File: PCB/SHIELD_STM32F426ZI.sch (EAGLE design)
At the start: 16 parts, among them IC1 AS4C16M16SA-6TCN

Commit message: Namen der DCMI-Pins hinzufügen und Position des Kondensators korrigieren
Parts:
- renumbered IC1 to SDRAM, STM32F4 to STM32

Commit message: new update
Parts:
- CAMERA, JP2, JP3: value (none) -> 0
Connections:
- new net PWDN: CAMERA.18, STM32G$6.PB5
- net CARD_DET: now also STM32G$6.PA5
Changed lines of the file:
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@@
 <part name="STM32" library="NUCLEO-F429ZI" deviceset="NUCLEO-F429ZI" device=""/>
 <part name="SDRAM" library="sdram" deviceset="AS4C16M16SA-6TCN" device=""/>
-<part name="CAMERA" library="pinhead" library_urn="urn:adsk.eagle:library:325" deviceset="PINHD-2X9" device="" package3d_urn="urn:adsk.eagle:package:22484/2"/>
-<part name="JP2" library="pinhead" library_urn="urn:adsk.eagle:library:325" deviceset="PINHD-1X2" device="" package3d_urn="urn:adsk.eagle:package:22435/2"/>
-<part name="JP3" library="pinhead" library_urn="urn:adsk.eagle:library:325" deviceset="PINHD-1X2" device="" package3d_urn="urn:adsk.eagle:package:22435/2"/>
+<part name="CAMERA" library="pinhead" library_urn="urn:adsk.eagle:library:325" deviceset="PINHD-2X9" device="" package3d_urn="urn:adsk.eagle:package:22484/2" value="0"/>
+<part name="JP2" library="pinhead" library_urn="urn:adsk.eagle:library:325" deviceset="PINHD-1X2" device="" package3d_urn="urn:adsk.eagle:package:22435/2" value="0"/>
+<part name="JP3" library="pinhead" library_urn="urn:adsk.eagle:library:325" deviceset="PINHD-1X2" device="" package3d_urn="urn:adsk.eagle:package:22435/2" value="0"/>
 <part name="C18" library="rcl" library_urn="urn:adsk.eagle:library:334" deviceset="C-EU" device="C0402K" package3d_urn="urn:adsk.eagle:package:23679/2" value="0.1uF"/>
 <part name="SUPPLY2" library="supply2" library_urn="urn:adsk.eagle:library:372" deviceset="GND" device=""/>
@@
 <instance part="CAMERA" gate="A" x="-20.32" y="25.4" smashed="yes">
 <attribute name="NAME" x="-26.67" y="38.735" size="1.778" layer="95"/>
-<attribute name="VALUE" x="-26.67" y="10.16" size="1.778" layer="96"/>
 </instance>
 <instance part="JP2" gate="G$1" x="30.48" y="33.02" smashed="yes">
 <attribute name="NAME" x="24.13" y="38.735" size="1.778" layer="95"/>
-<attribute name="VALUE" x="24.13" y="27.94" size="1.778" layer="96"/>
 </instance>
 <instance part="JP3" gate="G$1" x="30.48" y="20.32" smashed="yes">
 <attribute name="NAME" x="24.13" y="26.035" size="1.778" layer="95"/>
-<attribute name="VALUE" x="24.13" y="15.24" size="1.778" layer="96"/>
 </instance>
 <instance part="C18" gate="G$1" x="-58.42" y="129.54" smashed="yes">
@@
 </segment>
 </net>
+<net name="PWDN" class="0">
+<segment>
+<pinref part="STM32" gate="G$6" pin="PB5"/>
+<wire x1="124.46" y1="111.76" x2="137.16" y2="111.76" width="0.1524" layer="91"/>
+<wire x1="139.7" y1="111.76" x2="142.24" y2="111.76" width="0.1524" layer="91"/>
+<wire x1="139.7" y1="111.76" x2="137.16" y2="111.76" width="0.1524" layer="91"/>
+<label x="132.08" y="111.76" size="1.778" layer="95"/>
+<label x="132.08" y="111.76" size="1.778" layer="95"/>
+</segment>
+<segment>
+<pinref part="CAMERA" gate="A" pin="18"/>
+<wire x1="-15.24" y1="15.24" x2="2.54" y2="15.24" width="0.1524" layer="91"/>
+<label x="-7.62" y="15.24" size="1.778" layer="95"/>
+</segment>
+</net>
+<net name="CARD_DET" class="0">
+<segment>
+<pinref part="STM32" gate="G$6" pin="PA5"/>
+<wire x1="124.46" y1="134.62" x2="142.24" y2="134.62" width="0.1524" layer="91"/>
+<label x="132.08" y="134.62" size="1.778" layer="95"/>
+</segment>
+</net>

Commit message: new layout update
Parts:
- renumbered C18 to C1, R26 to R7, R27 to R5, R28 to R8, R29 to R4, R30 to R6, R31 to R9
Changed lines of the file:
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@@
 <part name="JP2" library="pinhead" library_urn="urn:adsk.eagle:library:325" deviceset="PINHD-1X2" device="" package3d_urn="urn:adsk.eagle:package:22435/2" value="0"/>
 <part name="JP3" library="pinhead" library_urn="urn:adsk.eagle:library:325" deviceset="PINHD-1X2" device="" package3d_urn="urn:adsk.eagle:package:22435/2" value="0"/>
-<part name="C18" library="rcl" library_urn="urn:adsk.eagle:library:334" deviceset="C-EU" device="C0402K" package3d_urn="urn:adsk.eagle:package:23679/2" value="0.1uF"/>
+<part name="C1" library="rcl" library_urn="urn:adsk.eagle:library:334" deviceset="C-EU" device="C0402K" package3d_urn="urn:adsk.eagle:package:23679/2" value="0.1uF"/>
 <part name="SUPPLY2" library="supply2" library_urn="urn:adsk.eagle:library:372" deviceset="GND" device=""/>
 <part name="GND7" library="supply1" library_urn="urn:adsk.eagle:library:371" deviceset="GND" device=""/>
 <part name="SDCARD" library="SamacSys_Parts" deviceset="104239-1430" device=""/>
-<part name="R26" library="rcl" library_urn="urn:adsk.eagle:library:334" deviceset="R-EU_" device="R0402" package3d_urn="urn:adsk.eagle:package:23547/3" value="100k"/>
-<part name="R27" library="rcl" library_urn="urn:adsk.eagle:library:334" deviceset="R-EU_" device="R0402" package3d_urn="urn:adsk.eagle:package:23547/3" value="100k"/>
-<part name="R28" library="rcl" library_urn="urn:adsk.eagle:library:334" deviceset="R-EU_" device="R0402" package3d_urn="urn:adsk.eagle:package:23547/3" value="100k"/>
-<part name="R29" library="rcl" library_urn="urn:adsk.eagle:library:334" deviceset="R-EU_" device="R0402" package3d_urn="urn:adsk.eagle:package:23547/3" value="100k"/>
-<part name="R30" library="rcl" library_urn="urn:adsk.eagle:library:334" deviceset="R-EU_" device="R0402" package3d_urn="urn:adsk.eagle:package:23547/3" value="100k"/>
-<part name="R31" library="rcl" library_urn="urn:adsk.eagle:library:334" deviceset="R-EU_" device="R0402" package3d_urn="urn:adsk.eagle:package:23547/3" value="100k"/>
+<part name="R7" library="rcl" library_urn="urn:adsk.eagle:library:334" deviceset="R-EU_" device="R0402" package3d_urn="urn:adsk.eagle:package:23547/3" value="100k"/>
+<part name="R5" library="rcl" library_urn="urn:adsk.eagle:library:334" deviceset="R-EU_" device="R0402" package3d_urn="urn:adsk.eagle:package:23547/3" value="100k"/>
+<part name="R8" library="rcl" library_urn="urn:adsk.eagle:library:334" deviceset="R-EU_" device="R0402" package3d_urn="urn:adsk.eagle:package:23547/3" value="100k"/>
+<part name="R4" library="rcl" library_urn="urn:adsk.eagle:library:334" deviceset="R-EU_" device="R0402" package3d_urn="urn:adsk.eagle:package:23547/3" value="100k"/>
+<part name="R6" library="rcl" library_urn="urn:adsk.eagle:library:334" deviceset="R-EU_" device="R0402" package3d_urn="urn:adsk.eagle:package:23547/3" value="100k"/>
+<part name="R9" library="rcl" library_urn="urn:adsk.eagle:library:334" deviceset="R-EU_" device="R0402" package3d_urn="urn:adsk.eagle:package:23547/3" value="100k"/>
 <part name="R1" library="sicom_universal" library_urn="urn:adsk.eagle:library:5101580" deviceset="R_0402" device="WEB_0402" package3d_urn="urn:adsk.eagle:package:23679/2" value="4.7k"/>
 <part name="R2" library="sicom_universal" library_urn="urn:adsk.eagle:library:5101580" deviceset="R_0402" device="WEB_0402" package3d_urn="urn:adsk.eagle:package:23679/2" value="4.7k"/>
@@
 <attribute name="NAME" x="24.13" y="26.035" size="1.778" layer="95"/>
 </instance>
-<instance part="C18" gate="G$1" x="-58.42" y="129.54" smashed="yes">
+<instance part="C1" gate="G$1" x="-58.42" y="129.54" smashed="yes">
 <attribute name="NAME" x="-56.896" y="129.921" size="1.778" layer="95"/>
 <attribute name="VALUE" x="-56.896" y="124.841" size="1.778" layer="96"/>
@@
 <label x="-55.88" y="149.86" size="1.9304" layer="95"/>
 <wire x1="-27.94" y1="137.16" x2="-58.42" y2="137.16" width="0.1524" layer="91"/>
-<pinref part="C18" gate="G$1" pin="1"/>
+<pinref part="C1" gate="G$1" pin="1"/>
 <wire x1="-58.42" y1="137.16" x2="-58.42" y2="132.08" width="0.1524" layer="91"/>
 <junction x="-58.42" y="137.16"/>
@@
 <segment>
 <pinref part="SUPPLY2" gate="GND" pin="GND"/>
-<pinref part="C18" gate="G$1" pin="2"/>
+<pinref part="C1" gate="G$1" pin="2"/>
 </segment>
 <segment>
@@
 <attribute name="VALUE" x="64.77" y="78.74" size="1.778" layer="96" align="center-left"/>
 </instance>
-<instance part="R26" gate="G$1" x="27.94" y="116.84" smashed="yes" rot="R270">
+<instance part="R7" gate="G$1" x="27.94" y="116.84" smashed="yes" rot="R270">
 <attribute name="NAME" x="29.4386" y="120.65" size="1.778" layer="95" rot="R270"/>
 <attribute name="VALUE" x="24.638" y="120.65" size="1.778" layer="96" rot="R270"/>
 </instance>
-<instance part="R27" gate="G$1" x="33.02" y="109.22" smashed="yes" rot="R270">
+<instance part="R5" gate="G$1" x="33.02" y="109.22" smashed="yes" rot="R270">
 <attribute name="NAME" x="34.5186" y="113.03" size="1.778" layer="95" rot="R270"/>
 <attribute name="VALUE" x="29.718" y="113.03" size="1.778" layer="96" rot="R270"/>
 </instance>
-<instance part="R28" gate="G$1" x="43.18" y="93.98" smashed="yes" rot="R270">
+<instance part="R8" gate="G$1" x="43.18" y="93.98" smashed="yes" rot="R270">
 <attribute name="NAME" x="44.6786" y="97.79" size="1.778" layer="95" rot="R270"/>
 <attribute name="VALUE" x="39.878" y="97.79" size="1.778" layer="96" rot="R270"/>
 </instance>
-<instance part="R29" gate="G$1" x="38.1" y="101.6" smashed="yes" rot="R270">
+<instance part="R4" gate="G$1" x="38.1" y="101.6" smashed="yes" rot="R270">
 <attribute name="NAME" x="39.5986" y="105.41" size="1.778" layer="95" rot="R270"/>
 <attribute name="VALUE" x="34.798" y="105.41" size="1.778" layer="96" rot="R270"/>
 </instance>
-<instance part="R30" gate="G$1" x="132.08" y="93.98" smashed="yes" rot="R270">
+<instance part="R6" gate="G$1" x="132.08" y="93.98" smashed="yes" rot="R270">
 <attribute name="NAME" x="133.5786" y="97.79" size="1.778" layer="95" rot="R270"/>
 <attribute name="VALUE" x="128.778" y="97.79" size="1.778" layer="96" rot="R270"/>
 </instance>
-<instance part="R31" gate="G$1" x="137.16" y="104.14" smashed="yes" rot="R270">
+<instance part="R9" gate="G$1" x="137.16" y="104.14" smashed="yes" rot="R270">
 <attribute name="NAME" x="138.6586" y="107.95" size="1.778" layer="95" rot="R270"/>
 <attribute name="VALUE" x="133.858" y="107.95" size="1.778" layer="96" rot="R270"/>
@@
 <label x="10.16" y="66.04" size="1.778" layer="95"/>
 <wire x1="60.96" y1="66.04" x2="27.94" y2="66.04" width="0.1524" layer="91"/>
-<pinref part="R26" gate="G$1" pin="2"/>
+<pinref part="R7" gate="G$1" pin="2"/>
 <wire x1="27.94" y1="66.04" x2="10.16" y2="66.04" width="0.1524" layer="91"/>
 <wire x1="27.94" y1="111.76" x2="27.94" y2="66.04" width="0.1524" layer="91"/>
@@
 <label x="10.16" y="63.5" size="1.778" layer="95"/>
 <wire x1="10.16" y1="63.5" x2="33.02" y2="63.5" width="0.1524" layer="91"/>
-<pinref part="R27" gate="G$1" pin="2"/>
+<pinref part="R5" gate="G$1" pin="2"/>
 <wire x1="33.02" y1="63.5" x2="60.96" y2="63.5" width="0.1524" layer="91"/>
 <wire x1="33.02" y1="104.14" x2="33.02" y2="63.5" width="0.1524" layer="91"/>
@@
 <label x="10.16" y="60.96" size="1.778" layer="95"/>
 <wire x1="60.96" y1="60.96" x2="38.1" y2="60.96" width="0.1524" layer="91"/>
-<pinref part="R29" gate="G$1" pin="2"/>
+<pinref part="R4" gate="G$1" pin="2"/>
 <wire x1="38.1" y1="60.96" x2="10.16" y2="60.96" width="0.1524" layer="91"/>
 <wire x1="38.1" y1="96.52" x2="38.1" y2="60.96" width="0.1524" layer="91"/>
@@
 <label x="10.16" y="58.42" size="1.778" layer="95"/>
 <wire x1="10.16" y1="58.42" x2="43.18" y2="58.42" width="0.1524" layer="91"/>
-<pinref part="R28" gate="G$1" pin="2"/>
+<pinref part="R8" gate="G$1" pin="2"/>
 <wire x1="43.18" y1="58.42" x2="60.96" y2="58.42" width="0.1524" layer="91"/>
 <wire x1="43.18" y1="88.9" x2="43.18" y2="58.42" width="0.1524" layer="91"/>
@@
 <wire x1="116.84" y1="58.42" x2="137.16" y2="58.42" width="0.1524" layer="91"/>
 <label x="147.32" y="58.42" size="1.778" layer="95"/>
-<pinref part="R31" gate="G$1" pin="2"/>
+<pinref part="R9" gate="G$1" pin="2"/>
 <wire x1="137.16" y1="58.42" x2="149.86" y2="58.42" width="0.1524" layer="91"/>
 <wire x1="137.16" y1="99.06" x2="137.16" y2="58.42" width="0.1524" layer="91"/>
@@
 <wire x1="116.84" y1="66.04" x2="132.08" y2="66.04" width="0.1524" layer="91"/>
 <label x="147.32" y="66.04" size="1.778" layer="95"/>
-<pinref part="R30" gate="G$1" pin="2"/>
+<pinref part="R6" gate="G$1" pin="2"/>
 <wire x1="132.08" y1="66.04" x2="149.86" y2="66.04" width="0.1524" layer="91"/>
 <wire x1="132.08" y1="88.9" x2="132.08" y2="66.04" width="0.1524" layer="91"/>
@@
 <net name="3.3V" class="0">
 <segment>
-<pinref part="R26" gate="G$1" pin="1"/>
+<pinref part="R7" gate="G$1" pin="1"/>
 <wire x1="27.94" y1="127" x2="27.94" y2="121.92" width="0.1524" layer="91"/>
-<pinref part="R27" gate="G$1" pin="1"/>
+<pinref part="R5" gate="G$1" pin="1"/>
 <wire x1="33.02" y1="127" x2="33.02" y2="114.3" width="0.1524" layer="91"/>
 <wire x1="27.94" y1="127" x2="33.02" y2="127" width="0.1524" layer="91"/>
-<pinref part="R29" gate="G$1" pin="1"/>
+<pinref part="R4" gate="G$1" pin="1"/>
 <wire x1="38.1" y1="106.68" x2="38.1" y2="127" width="0.1524" layer="91"/>
 <wire x1="33.02" y1="127" x2="38.1" y2="127" width="0.1524" layer="91"/>
 <junction x="33.02" y="127"/>
-<pinref part="R28" gate="G$1" pin="1"/>
+<pinref part="R8" gate="G$1" pin="1"/>
 <wire x1="43.18" y1="127" x2="43.18" y2="99.06" width="0.1524" layer="91"/>
 <wire x1="38.1" y1="127" x2="43.18" y2="127" width="0.1524" layer="91"/>
@@
 </segment>
 <segment>
-<pinref part="R30" gate="G$1" pin="1"/>
+<pinref part="R6" gate="G$1" pin="1"/>
 <wire x1="132.08" y1="99.06" x2="132.08" y2="127" width="0.1524" layer="91"/>
-<pinref part="R31" gate="G$1" pin="1"/>
+<pinref part="R9" gate="G$1" pin="1"/>
 <wire x1="137.16" y1="127" x2="137.16" y2="109.22" width="0.1524" layer="91"/>
 <wire x1="132.08" y1="127" x2="137.16" y2="127" width="0.1524" layer="91"/>

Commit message: add mosfet and fix GPIOs for sdram and sdcard
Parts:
- removed JP2, JP3: 0, pinhead:PINHD-1X2
- added Q1: FDN304P, FDN304P:FDN304P
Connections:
- removed net FMC_SDCKE0: SDRAM.CKE, STM32G$5.PC3
- removed net FMC_SDNE0: R3.1, SDRAM.CS#, STM32G$5.PC2
- removed net I2C1_SCL: CAMERA.3, R2.1, STM32G$6.PB6
- removed net I2C1_SDA: CAMERA.4, R1.1, STM32G$5.PB7
- new net FMC_SDCKE1: SDRAM.CKE, STM32G$6.PB5
- new net FMC_SDNE1: R3.1, SDRAM.CS#, STM32G$6.PB6
- new net GATE: Q1.G, STM32G$5.PC2
- new net I2C2_SCL: CAMERA.3, R2.1, STM32G$6.PB10
- new net I2C2_SDA: CAMERA.4, R1.1, STM32G$6.PB11
- new net RESET: CAMERA.17, STM32G$6.PB3
- net 3.3: now also Q1.D; no longer JP2.2
- net 3.3V: now also Q1.S; no longer JP2.1
- net DCMI_D2: now also STM32G$5.PG10; no longer STM32G$6.PE0
- net DCMI_D3: now also STM32G$5.PG11; no longer STM32G$5.PE1
- net DCMI_VSYNC: now also STM32G$5.PB7; no longer STM32G$5.PG9
- net LDQM: now also STM32G$6.PE0; no longer JP3.1
- net PWDN: now also STM32G$6.PB4; no longer STM32G$6.PB5
- net UDQM: now also STM32G$5.PE1; no longer JP3.2

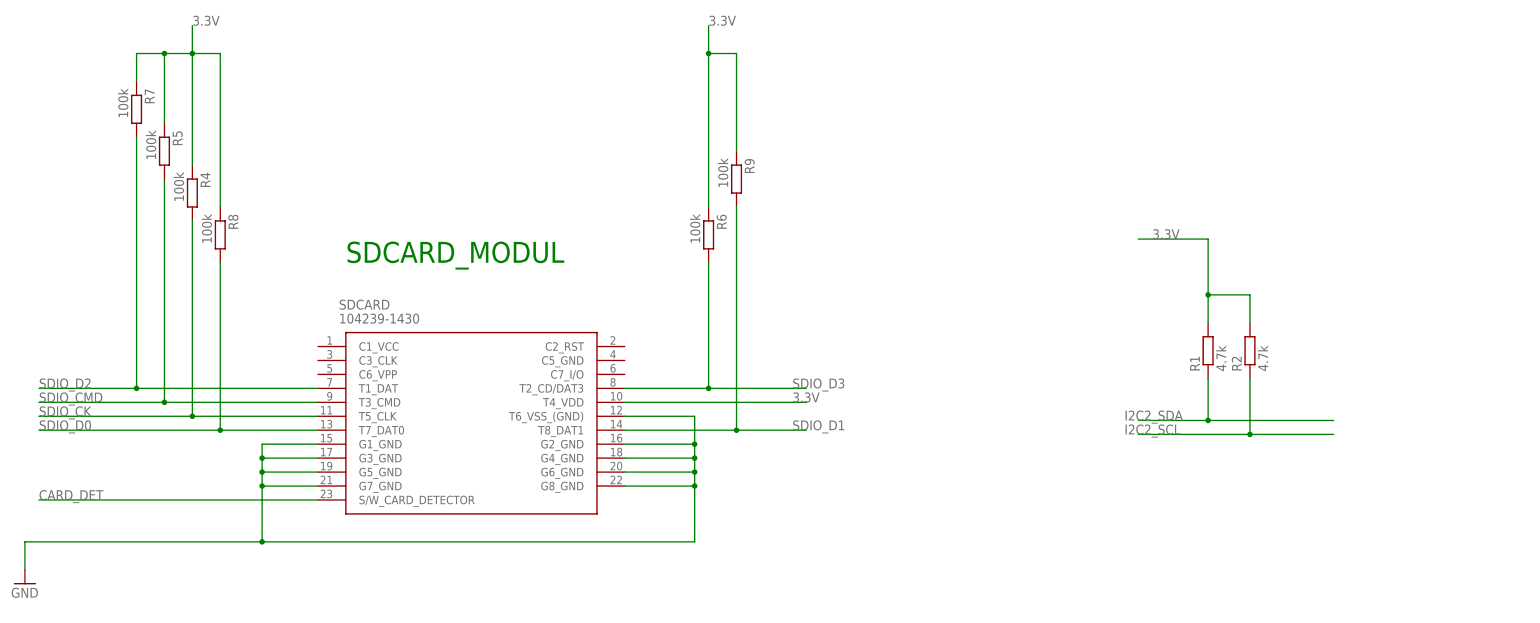
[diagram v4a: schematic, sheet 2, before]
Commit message: new position camrera and pir sensor
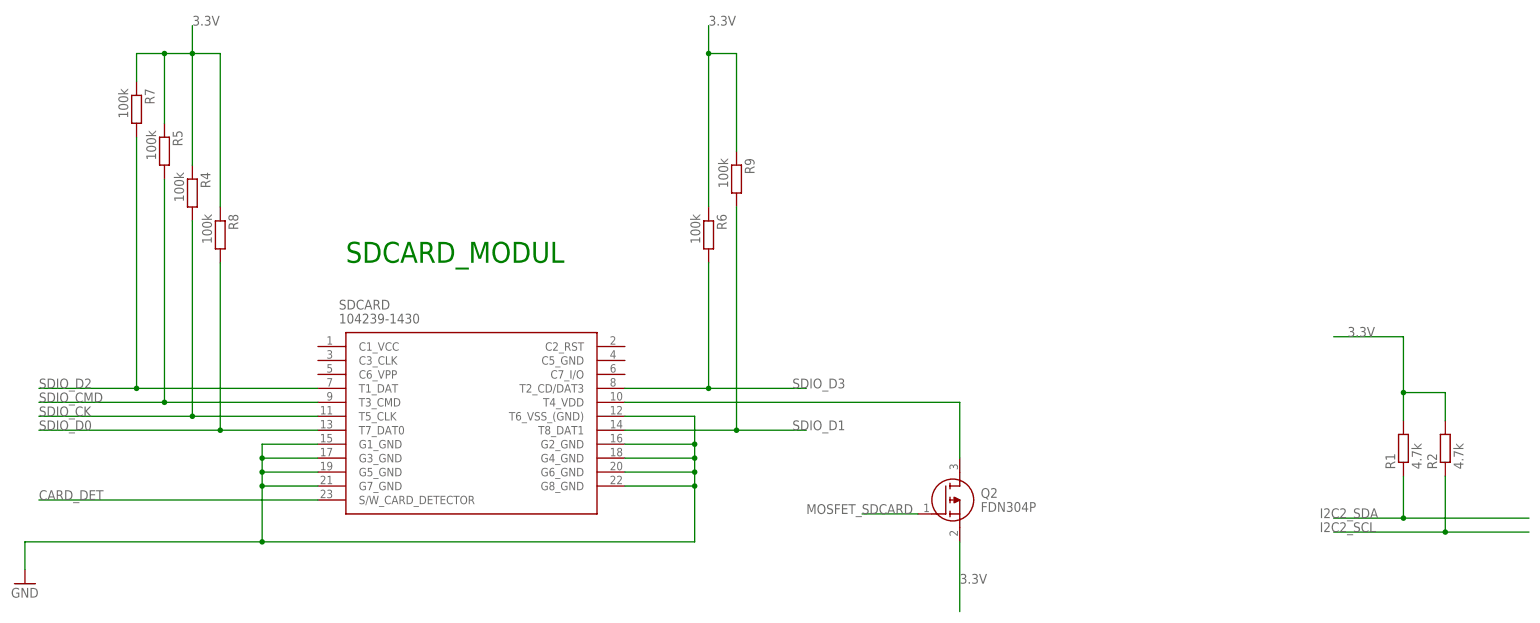
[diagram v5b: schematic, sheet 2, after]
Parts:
- added PIR: SENBA_PIR_3PIN, sicom_universal:SENBA_PIR_3PIN
- added Q2: FDN304P, FDN304P:FDN304P
- added Q4: SSM3J338R,LF, SamacSys_Parts:SSM3J338R,LF
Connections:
- new net MOSFET_SDCARD: Q2.G, STM32G$5.PA1
- new net N$1: Q2.D, SDCARD.T4_VDD
- new net PIR_3V3: PIR.2, Q4.D
- new net PIR_EN: Q4.G, STM32G$5.PG13
- new net PIR_INT: PIR.1, STM32G$5.PG12
- net 3.3V: now also Q2.S, Q4.S; no longer SDCARD.T4_VDD
- net DCMI_D0: now also STM32G$6.PA9; no longer STM32G$6.PC6
- net DCMI_D1: now also STM32G$6.PA10; no longer STM32G$6.PC7
- net GATE: now also STM32G$5.PG9; no longer STM32G$5.PC2
- net GND: now also PIR.3
- net PWDN: now also STM32G$6.PB3; no longer STM32G$6.PB4
- net RESET: now also STM32G$6.PB4; no longer STM32G$6.PB3
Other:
- note added: "PIR"
- moved on the sheet: R1, R2

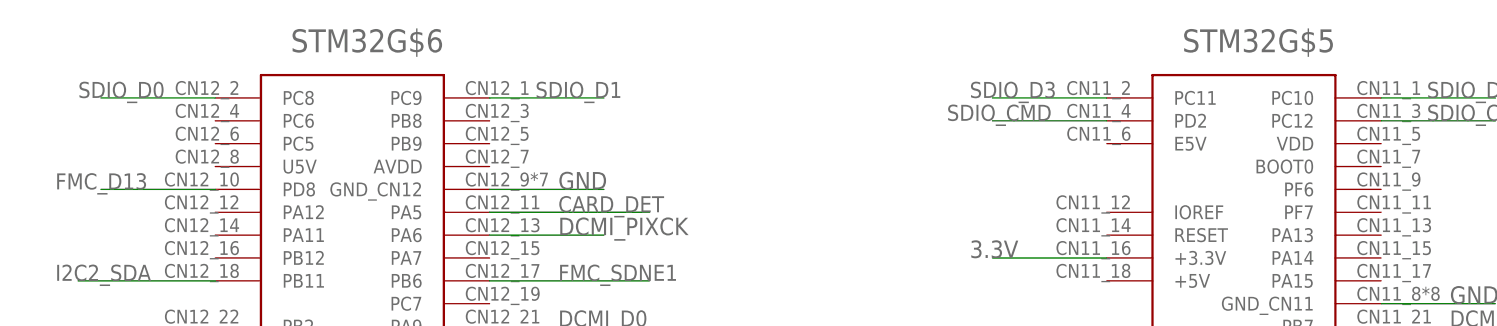
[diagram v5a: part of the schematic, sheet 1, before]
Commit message: new position camera and add pir sensor
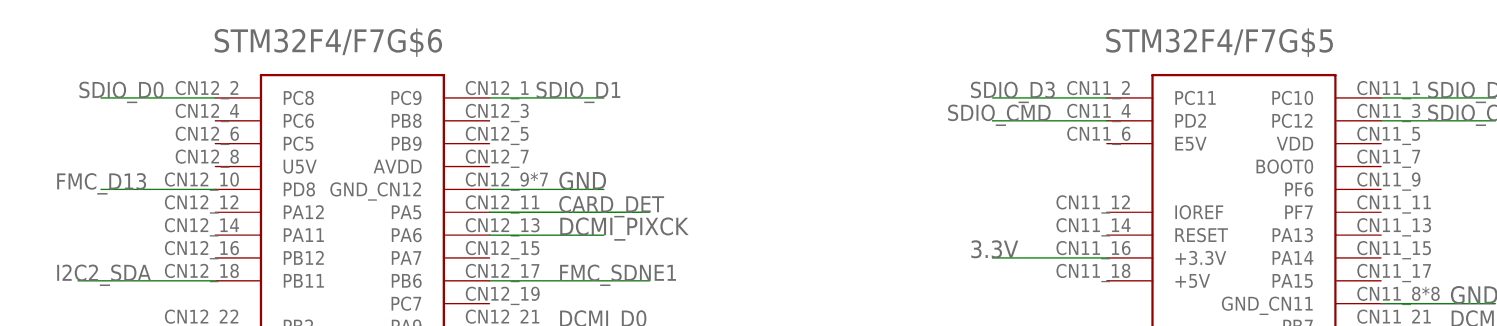
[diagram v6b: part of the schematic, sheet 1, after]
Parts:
- renumbered STM32 to STM32F4/F7

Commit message: fix route
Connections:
- net CARD_DET: now also STM32F4/F7G$6.PB8; no longer STM32F4/F7G$6.PA5
- net MOSFET_SDCARD: now also STM32F4/F7G$5.PA13; no longer STM32F4/F7G$5.PA1
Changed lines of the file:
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@@
-</segment>
-</net>
-<net name="CARD_DET" class="0">
-<segment>
-<pinref part="STM32F4/F7" gate="G$6" pin="PA5"/>
-<wire x1="124.46" y1="134.62" x2="142.24" y2="134.62" width="0.1524" layer="91"/>
-<label x="132.08" y="134.62" size="1.778" layer="95"/>
 </segment>
 </net>
@@
 <net name="MOSFET_SDCARD" class="0">
 <segment>
-<pinref part="STM32F4/F7" gate="G$5" pin="PA1"/>
-<wire x1="193.04" y1="111.76" x2="177.8" y2="111.76" width="0.1524" layer="91"/>
-<label x="165.1" y="111.76" size="1.778" layer="95"/>
+<pinref part="STM32F4/F7" gate="G$5" pin="PA13"/>
+<wire x1="223.52" y1="132.08" x2="241.3" y2="132.08" width="0.1524" layer="91"/>
 </segment>
 </net>
+<net name="CARD_DET" class="0">
+<segment>
+<pinref part="STM32F4/F7" gate="G$6" pin="PB8"/>
+<wire x1="124.46" y1="144.78" x2="139.7" y2="144.78" width="0.1524" layer="91"/>
+</segment>
+</net>
